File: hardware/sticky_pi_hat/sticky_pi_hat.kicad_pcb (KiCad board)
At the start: 2 copper layers, 65 x 45 mm, 27 parts, among them J1 Screw_Terminal_01x11, J2 Conn_02x13_Odd_Even, J3 Conn_01x02_Male, Q1 BSS806NH6327XTSA1, U2 TPL5110, U3 TPS63002, U4 DS1307Z+, Y1 Crystal

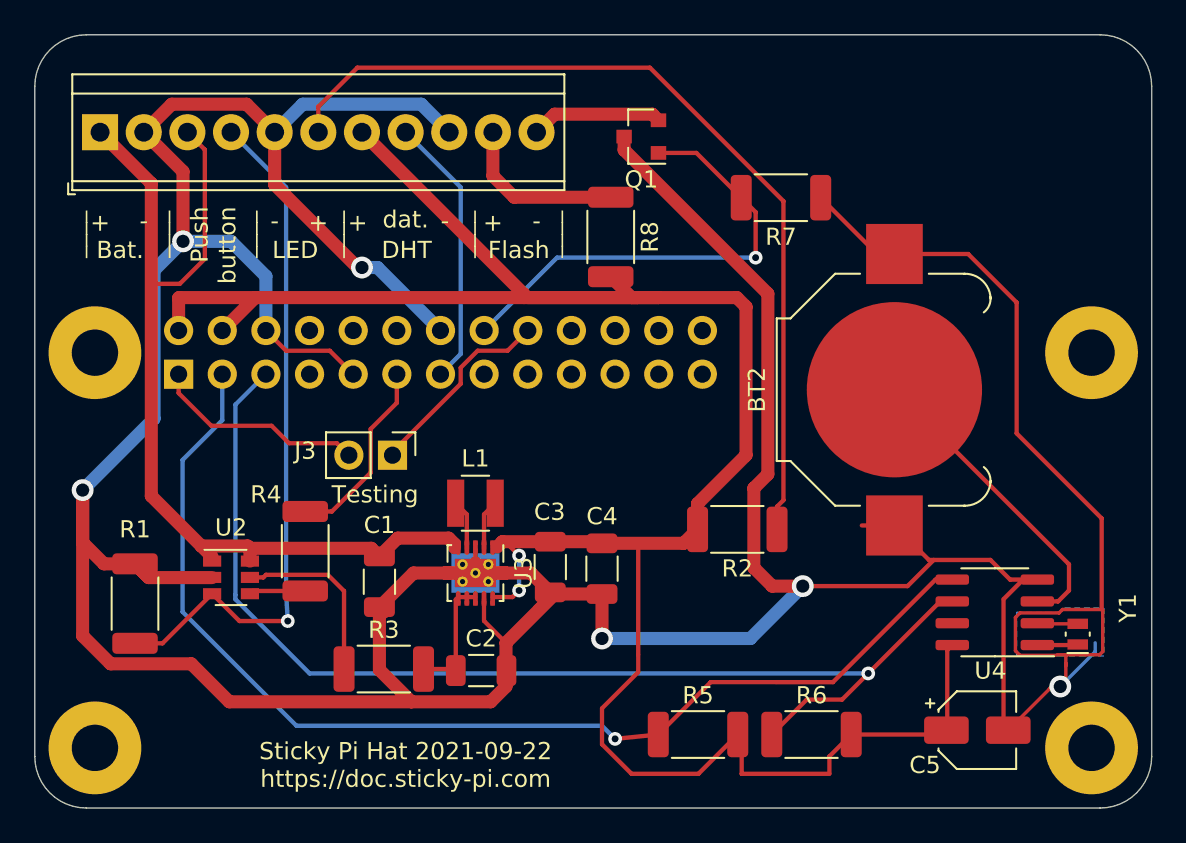
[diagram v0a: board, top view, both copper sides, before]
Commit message: Add P-channel mosfet to tpl5110
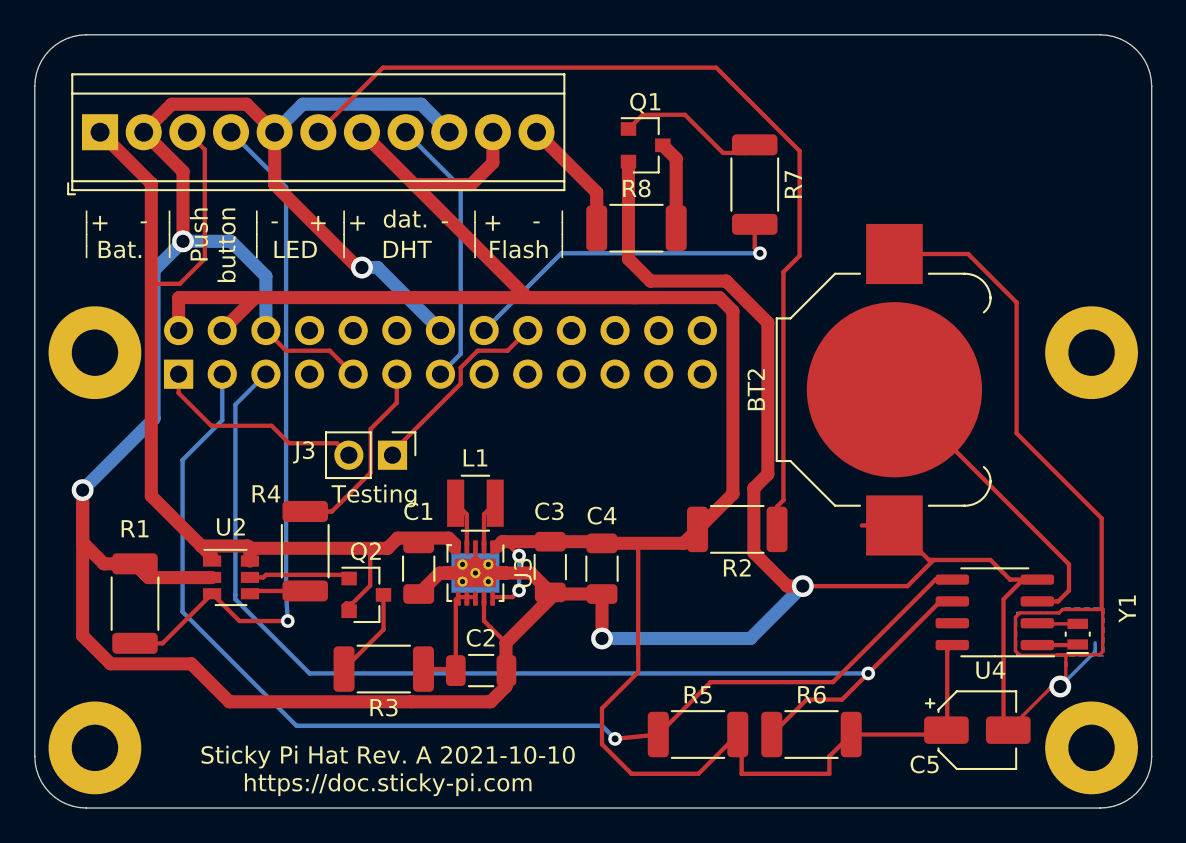
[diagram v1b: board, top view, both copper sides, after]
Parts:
- added Q2: DMP2045U, Package_TO_SOT_SMD:SOT-23, F.Cu at (129.8, 117.1)
- moved C1 2.41 mm to (132.8, 115.6)
- moved R7 1.70 mm to (152.4, 93.2), turned to 270 degrees
- moved R8 1.58 mm to (145.5, 95.8), turned to 0 degrees
- moved Q1 0.57 mm to (146.1, 90.9), turned to 0 degrees
- turned R3 to 180 degrees
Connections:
- J1 pad 10: Net-(D1-Pad2) -> +5V
- Q1 pad 1: Net-(J2-Pad16) -> Net-(Q1-Pad1)
- Q1 pad 2: Net-(D1-Pad1) -> Earth
- Q1 pad 3: Earth -> Net-(Q1-Pad3)
- R3 pad 1: Net-(R3-Pad1) -> Net-(C2-Pad2)
- R3 pad 2: Net-(C2-Pad2) -> Net-(Q2-Pad3)
- R7 pad 1: Earth -> Net-(Q1-Pad1)
- R8 pad 1: Net-(D1-Pad2) -> Net-(D1-Pad1)
- R8 pad 2: +5V -> Net-(Q1-Pad3)
- U2 pad 5: Net-(R3-Pad1) -> Net-(Q2-Pad1)
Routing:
- net Earth: track 296.0 -> 282.7 mm
- net Net-(R3-Pad1): track 10.5 -> 0.00 mm
- net Net-(D1-Pad2): track 9.91 -> 0.00 mm
- net Net-(Q1-Pad1): track 0.00 -> 8.81 mm
- net Net-(J2-Pad16): track 27.6 -> 19.7 mm
- net Net-(Q2-Pad3): track 0.00 -> 6.02 mm
- net Net-(Q2-Pad1): track 0.00 -> 5.87 mm
- net Net-(Q1-Pad3): track 0.00 -> 5.15 mm
- net +5V: track 135.1 -> 139.0 mm
- net Net-(BT1-Pad1): track 55.4 -> 59.3 mm
- net Net-(D2-Pad2): track 52.0 -> 54.1 mm
- net Net-(D1-Pad1): track 7.68 -> 7.04 mm
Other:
- board text added: "Sticky Pi Hat Rev. A 2021-10-10 https://doc.sticky-pi.com"
- board text removed: "Sticky Pi Hat 2021-09-22 https://doc.sticky-pi.com"

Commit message: update
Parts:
- removed the REF** at (172.0, 103.0)
- removed the REF** at (114.0, 103.0)
- removed the REF** at (172.0, 126.0)
- removed the REF** at (114.0, 126.0)
- added C6: 10μF, Capacitor_SMD:C_1206_3216Metric, F.Cu at (142.3, 123.1)
- added D3: SM4001PL, Diode_SMD:D_SOD-123F, F.Cu at (120.4, 122.3)
- added G***: LOGO, logo:logo-doc, B.Cu at (161.0, 108.0)
- added G***: LOGO, logo:logo, F.Cu at (168.9, 91.2)
- added Q3: BSS806NH6327XTSA1, Package_TO_SOT_SMD:SOT-23, F.Cu at (125.1, 121.0)
- added Q4: BSS806NH6327XTSA1, Package_TO_SOT_SMD:SOT-23, F.Cu at (140.5, 111.4)
- added R10: 75k, Resistor_SMD:R_2010_5025Metric, F.Cu at (132.4, 109.9)
- added R9: 49.9k, Resistor_SMD:R_0805_2012Metric, F.Cu at (137.7, 107.7)
- added REF**: MountingHole_3.2mm_M3_DIN965_Pad, MountingHole:MountingHole_3.2mm_M3_DIN965_Pad, F.Cu at (172.0, 126.0)
- added REF**: MountingHole_3.2mm_M3_DIN965_Pad, MountingHole:MountingHole_3.2mm_M3_DIN965_Pad, F.Cu at (172.0, 103.0)
- added REF**: MountingHole_3.2mm_M3_DIN965_Pad, MountingHole:MountingHole_3.2mm_M3_DIN965_Pad, F.Cu at (114.0, 126.0)
- added REF**: MountingHole_3.2mm_M3_DIN965_Pad, MountingHole:MountingHole_3.2mm_M3_DIN965_Pad, F.Cu at (114.0, 103.0)
- added U5: MCP3001-I_ST, Microchip-MCP3001-I_ST-*:Microchip-MCP3001-I_ST-Level_A, F.Cu at (146.0, 107.4)
- Q2: value DMP2045U -> AO3415A
- moved J3 4.89 mm to (126.4, 108.7)
- moved R6 2.99 mm to (158.1, 123.5)
- moved R5 2.21 mm to (150.2, 123.3)
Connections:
- net Net-(BT1-Pad1) renamed +BATT
- net Net-(J1-Pad4) renamed push_button
- net Net-(J1-Pad8) renamed GPIO_27
- net Net-(J2-Pad16) renamed GPIO_23
- net Net-(J2-Pad3) renamed GPIO_2
- net Net-(J2-Pad5) renamed GPIO_3
- net Net-(Q2-Pad1) renamed drv
- net Net-(R4-Pad1) renamed GPIO_17_R
- BT2 pad 1: Earth -> Net-(BT2-Pad1)
- BT2 pad 2: Net-(BT2-Pad2) -> Earth
- J2 pad 15: Net-(J2-Pad15) -> GPIO_22
- J2 pad 21: Net-(J2-Pad21) -> GPIO_9_MISO
- J2 pad 23: Net-(J2-Pad23) -> GPIO_11_clk
- J2 pad 24: Net-(J2-Pad24) -> GPIO_8_C0
- U4 pad 3: Net-(BT2-Pad2) -> Net-(BT2-Pad1)
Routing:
- net Net-(C6-Pad1): track 0.00 -> 50.9 mm, vias 0 -> 5
- net Net-(BT2-Pad1): track 0.00 -> 38.5 mm
- net +3V3: track 12.5 -> 49.2 mm, vias 0 -> 2
- net Earth: track 282.7 -> 310.9 mm, vias 6 -> 7
- net Net-(BT2-Pad2): track 18.0 -> 0.00 mm
- net drv: track 5.87 -> 23.5 mm, vias 0 -> 2
- net Net-(R10-Pad1): track 0.00 -> 17.2 mm
- net GPIO_8_C0: track 0.00 -> 13.2 mm
- net GPIO_22: track 0.00 -> 7.50 mm
- net GPIO_9_MISO: track 0.00 -> 6.63 mm
- net GPIO_11_clk: track 0.00 -> 4.93 mm
- net Net-(J2-Pad18): track 11.5 -> 16.2 mm
- net +5V: track 139.0 -> 134.6 mm
- net GPIO_17_R: track 3.28 -> 7.30 mm
- net GPIO_3: track 66.2 -> 63.3 mm
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
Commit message: add external pull down resistor to flash and push button outputs
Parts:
- added C7: 47uF, Capacitor_SMD:CP_Elec_5x5.3, F.Cu at (115.9, 114.1)
- added R11: 10k, Resistor_SMD:R_2010_5025Metric, F.Cu at (117.6, 109.0)
- added R12: 10k, Resistor_SMD:R_2010_5025Metric, F.Cu at (157.7, 90.8)
- moved R1 2.79 mm to (115.8, 120.3), turned to 180 degrees
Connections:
- Q2 pad 3: Net-(Q2-Pad3) -> batt_io
- R3 pad 2: Net-(Q2-Pad3) -> batt_io
- R9 pad 1: drv -> batt_io
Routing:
- net batt_io: track 0.00 -> 19.9 mm, vias 0 -> 2
- net Earth: track 310.9 -> 329.2 mm
- net drv: track 23.5 -> 6.02 mm, vias 2 -> 0
- net Net-(J2-Pad11): track 12.8 -> 20.4 mm
- net Net-(Q2-Pad3): track 6.02 -> 0.00 mm
- net GPIO_23: track 19.7 -> 25.7 mm
- net Net-(D2-Pad2): track 54.1 -> 59.2 mm
- net Net-(C6-Pad1): track 50.9 -> 49.3 mm
- net +BATT: track 58.4 -> 60.0 mm
- net push_button: track 41.8 -> 40.5 mm
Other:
- board text added: "Sticky Pi Hat Rev. B 2021-12-15 https://doc.sticky-pi.com"
- board text removed: "Sticky Pi Hat Rev. A 2021-10-10 https://doc.sticky-pi.com"

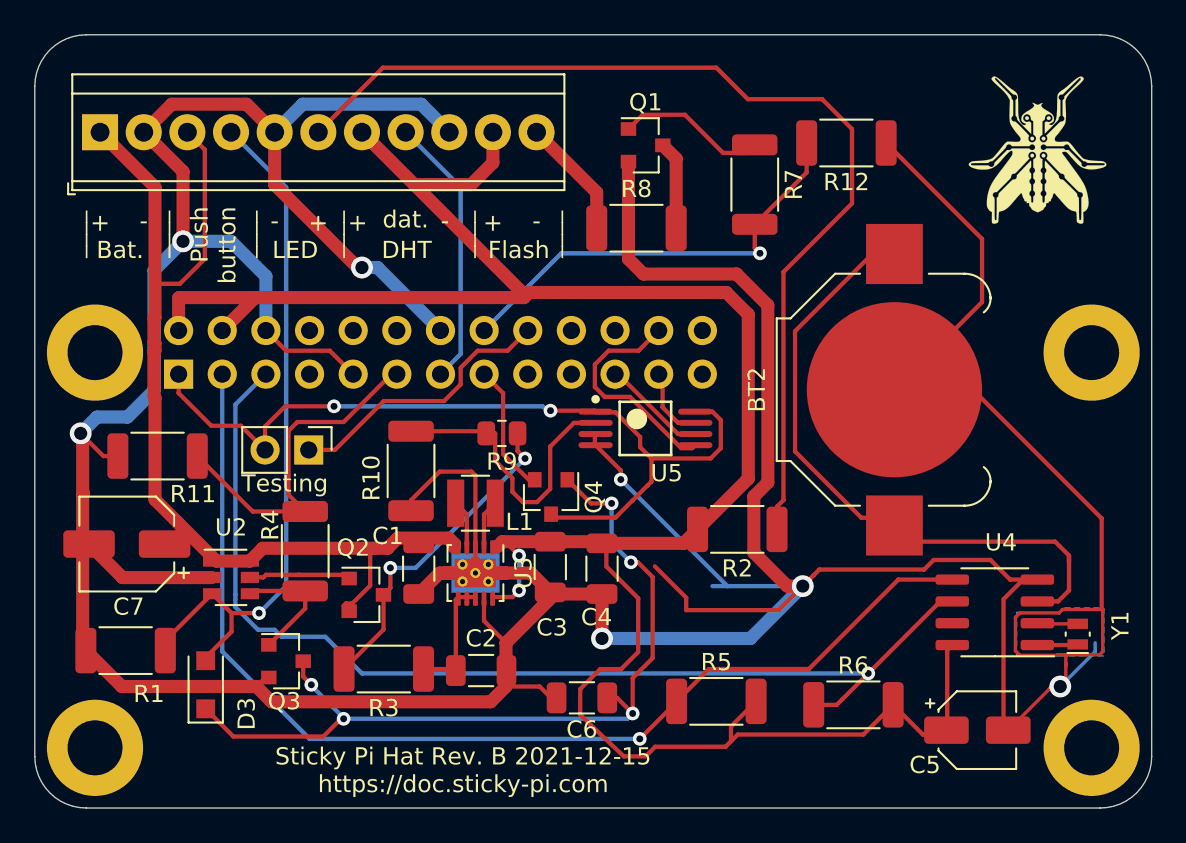
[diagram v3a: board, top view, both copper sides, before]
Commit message: add diode to prevent wrong measurement of R1(timing) dut to pushbutton state holder
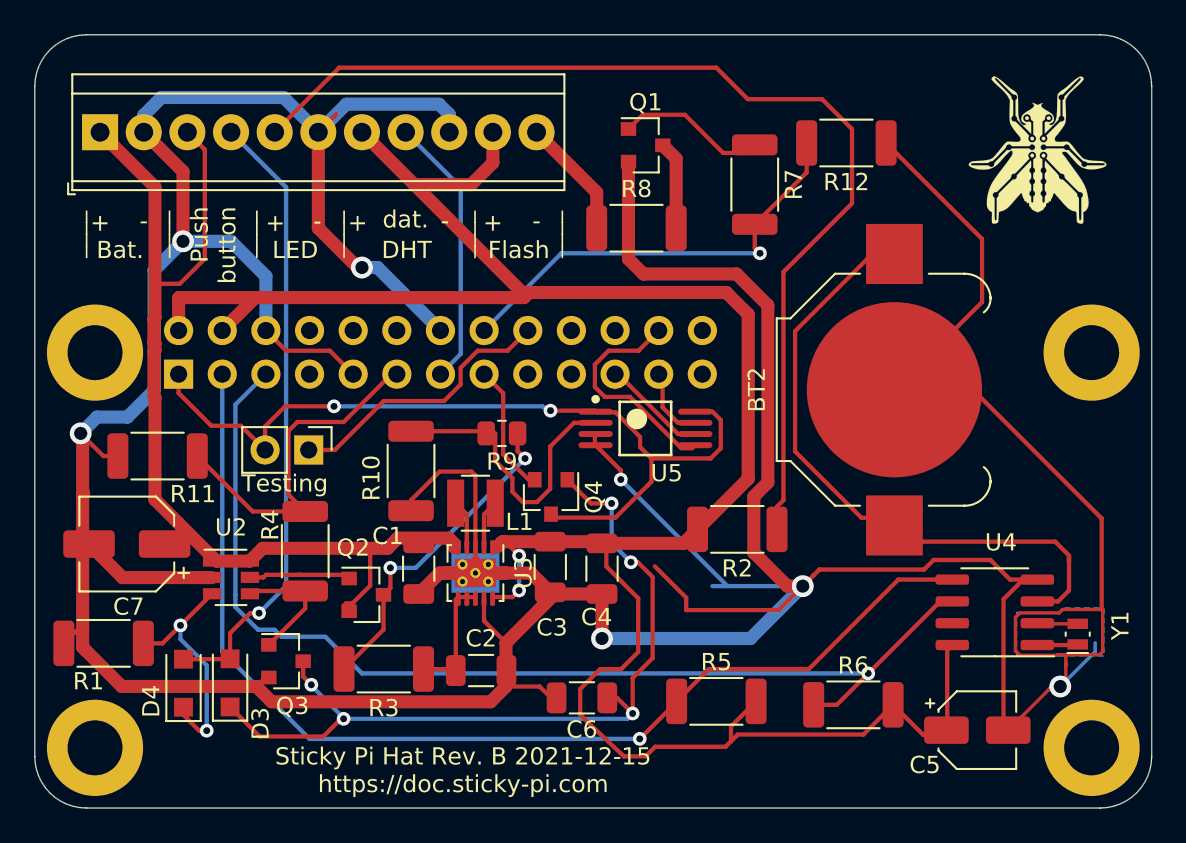
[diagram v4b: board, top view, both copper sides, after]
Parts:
- added D4: SM4001PL, Diode_SMD:D_SOD-123F, F.Cu at (119.2, 122.2)
- moved D3 1.42 mm to (121.9, 122.2)
- moved R1 1.35 mm to (114.5, 119.9)
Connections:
- J1 pad 5: Earth -> Net-(D2-Pad2)
- J1 pad 6: Net-(D2-Pad2) -> Earth
- R1 pad 1: push_button -> Net-(D4-Pad1)
- U2 pad 3: push_button -> Net-(D4-Pad1)
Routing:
- net Net-(D4-Pad1): track 0.00 -> 14.1 mm, vias 0 -> 2
- net push_button: track 40.5 -> 36.3 mm
- net Earth: track 329.2 -> 332.5 mm
- net Net-(D2-Pad2): track 59.2 -> 61.7 mm
- net Net-(C6-Pad1): track 49.3 -> 48.0 mm

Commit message: hardware updates
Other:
- net class Default removed
